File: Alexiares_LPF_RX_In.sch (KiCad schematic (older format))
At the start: 21 parts, among them J1 CONN_COAXIAL, J2 CONN_COAXIAL, J3 Conn_01x03, J5 CONN_COAXIAL

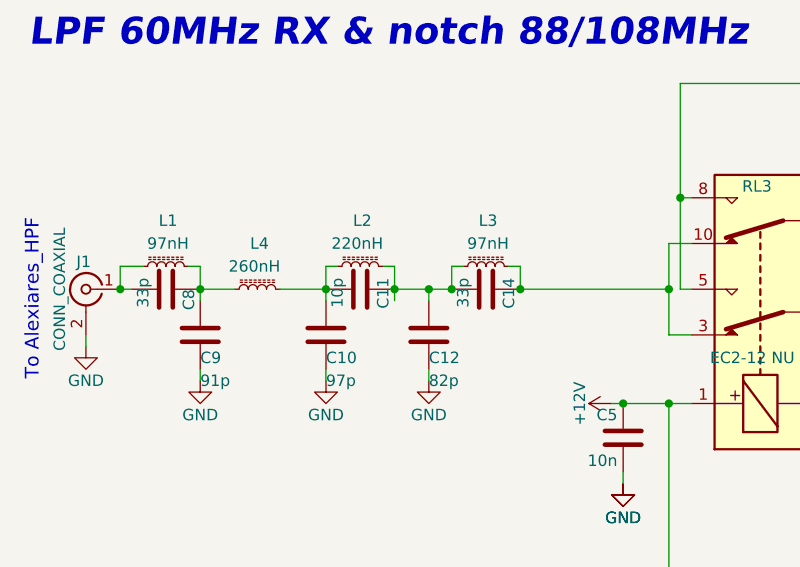
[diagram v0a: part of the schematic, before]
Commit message: Caps changed for ATC footprint
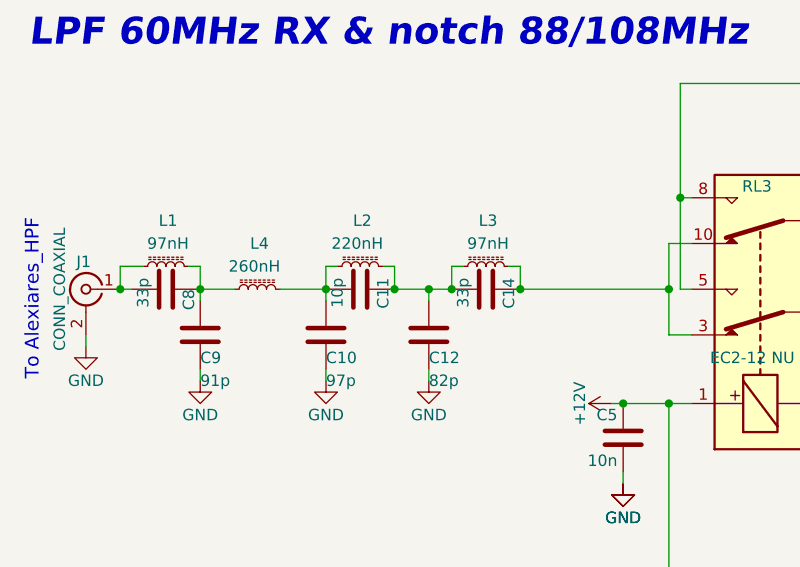
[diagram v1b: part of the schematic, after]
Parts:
- C10, C11, C12, C14, C8, C9: footprint Capacitors_SMD:C_1206_HandSoldering -> ATC_B:ATC_500_HandSoldering
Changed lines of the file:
@@
 F 0 "C14" H 3700 3900 50  0000 L CNN
 F 1 "33p" H 3700 3700 50  0000 L CNN
-F 2 "Capacitors_SMD:C_1206_HandSoldering" H 3788 3650 50  0001 C CNN
+F 2 "ATC_B:ATC_500_HandSoldering" H 3788 3650 50  0001 C CNN
 F 3 "" H 3750 3800 50  0000 C CNN
 	1    3750 3800
@@
 F 0 "C8" H 2350 3900 50  0000 L CNN
 F 1 "33p" H 2300 3700 50  0000 L CNN
-F 2 "Capacitors_SMD:C_1206_HandSoldering" H 2388 3650 50  0001 C CNN
+F 2 "ATC_B:ATC_500_HandSoldering" H 2388 3650 50  0001 C CNN
 F 3 "" H 2350 3800 50  0000 C CNN
 	1    2350 3800
@@
 F 0 "C11" H 3150 3900 50  0000 L CNN
 F 1 "10p" H 3150 3700 50  0000 L CNN
-F 2 "Capacitors_SMD:C_1206_HandSoldering" H 3238 3650 50  0001 C CNN
+F 2 "ATC_B:ATC_500_HandSoldering" H 3238 3650 50  0001 C CNN
 F 3 "" H 3200 3800 50  0000 C CNN
 	1    3200 3800
@@
 F 0 "C9" H 2500 3900 50  0000 L CNN
 F 1 "91p" H 2500 3800 50  0000 L CNN
-F 2 "Capacitors_SMD:C_1206_HandSoldering" H 2538 3850 50  0001 C CNN
+F 2 "ATC_B:ATC_500_HandSoldering" H 2538 3850 50  0001 C CNN
 F 3 "" H 2500 4000 50  0000 C CNN
 	1    2500 4000
@@
 F 0 "C10" H 3050 3900 50  0000 L CNN
 F 1 "97p" H 3050 3800 50  0000 L CNN
-F 2 "Capacitors_SMD:C_1206_HandSoldering" H 3088 3850 50  0001 C CNN
+F 2 "ATC_B:ATC_500_HandSoldering" H 3088 3850 50  0001 C CNN
 F 3 "" H 3050 4000 50  0000 C CNN
 	1    3050 4000
@@
 F 0 "C12" H 3500 3900 50  0000 L CNN
 F 1 "82p" H 3500 3800 50  0000 L CNN
-F 2 "Capacitors_SMD:C_1206_HandSoldering" H 3538 3850 50  0001 C CNN
+F 2 "ATC_B:ATC_500_HandSoldering" H 3538 3850 50  0001 C CNN
 F 3 "" H 3500 4000 50  0000 C CNN
 	1    3500 4000
@@
 Wire Wire Line
 	3050 3700 3050 3850
-Wire Wire Line
-	3350 3700 3350 3850
 Wire Wire Line
 	3350 3800 3600 3800
@@
 Text Notes 7600 4900 0    197  ~ 39
 Ajouter ferrites \nsur le relais
+Wire Wire Line
+	3350 3700 3350 3800
 $EndSCHEMATC

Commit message: DEPRECATED PROJECT, DO NOT USE WITH ALEX
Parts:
- added J4, J6, J7: CONN_COAXIAL, SMA_PINS:SMA_EDGE_NRW, symbol Conn_Coaxial
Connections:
- net GND: now also J4.2 (Ext), J6.2 (Ext), J7.2 (Ext)
- net at J2.1 (In), RL3.4, RL3.9: now also J7.1 (In)
- net at J5.1 (In), RL3.5, RL3.8: now also J6.1 (In)
- net at C8.2, J1.1 (In), L1.1: now also J4.1 (In)
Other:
- note added: "This project is deprecated\ndo no use on Angelia/Alexiares \n"
- note removed: "HPF \nOut"
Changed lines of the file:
@@
 Text Notes 8150 15900 0    60   ~ 0
 May 22nd 2017
-Text Notes 5700 3900 0    60   ~ 12
+Text Notes 6050 3900 0    60   ~ 12
 RX1_Line\n\n
-Text Notes 7800 14600 0    197  ~ 39
-HPF \nOut
+Text Notes 1700 2450 0    197  ~ 39
+This project is deprecated\ndo no use on Angelia/Alexiares \n
 Wire Wire Line
 	5500 4000 5500 4050
@@
 	3900 3800 4550 3800
 Wire Wire Line
-	2150 3700 2250 3700
+	1900 3700 2250 3700
 Wire Wire Line
 	2450 3700 2500 3700
@@
 	-1   0    0    -1
 $EndComp
-Text Notes 1800 4200 1    60   ~ 0
+Text Notes 1400 4050 1    60   ~ 0
 To Alexiares_HPF
 $Comp
@@
 Wire Wire Line
 	3350 3700 3350 3800
+Wire Wire Line
+	5300 3250 5300 3300
+$Comp
+L GND #PWR022
+U 1 1 5A34F329
+P 5300 3300
+F 0 "#PWR022" H 5300 3050 50  0001 C CNN
+F 1 "GND" H 5300 3150 50  0000 C CNN
+F 2 "" H 5300 3300 50  0000 C CNN
+F 3 "" H 5300 3300 50  0000 C CNN
+	1    5300 3300
+	-1   0    0    -1
+$EndComp
+$Comp
+L Conn_Coaxial J6
+U 1 1 5A34F32F
+P 5300 3050
+F 0 "J6" H 5310 3170 50  0000 C CNN
+F 1 "CONN_COAXIAL" V 5415 3050 50  0000 C CNN
+F 2 "SMA_PINS:SMA_EDGE_NRW" H 5300 3050 50  0001 C CNN
+F 3 "" H 5300 3050 50  0001 C CNN
+	1    5300 3050
+	1    0    0    -1
+$EndComp
+Wire Wire Line
+	5750 4000 5750 4050
+$Comp
+L GND #PWR023
+U 1 1 5A34F40A
+P 5750 4050
+F 0 "#PWR023" H 5750 3800 50  0001 C CNN
+F 1 "GND" H 5750 3900 50  0000 C CNN
+F 2 "" H 5750 4050 50  0000 C CNN
+F 3 "" H 5750 4050 50  0000 C CNN
+	1    5750 4050
+	-1   0    0    -1
+$EndComp
+$Comp
+L Conn_Coaxial J7
+U 1 1 5A34F410
+P 5750 3800
+F 0 "J7" H 5760 3920 50  0000 C CNN
+F 1 "CONN_COAXIAL" V 5865 3800 50  0000 C CNN
+F 2 "SMA_PINS:SMA_EDGE_NRW" H 5750 3800 50  0001 C CNN
+F 3 "" H 5750 3800 50  0001 C CNN
+	1    5750 3800
+	1    0    0    -1
+$EndComp
+Wire Wire Line
+	1750 4000 1750 4050
+$Comp
+L GND #PWR024
+U 1 1 5A34F599
+P 1750 4050
+F 0 "#PWR024" H 1750 3800 50  0001 C CNN
+F 1 "GND" H 1750 3900 50  0000 C CNN
+F 2 "" H 1750 4050 50  0000 C CNN
+F 3 "" H 1750 4050 50  0000 C CNN
+	1    1750 4050
+	1    0    0    -1
+$EndComp
+$Comp
+L Conn_Coaxial J4
+U 1 1 5A34F59F
+P 1750 3800
+F 0 "J4" H 1760 3920 50  0000 C CNN
+F 1 "CONN_COAXIAL" V 1865 3800 50  0000 C CNN
+F 2 "SMA_PINS:SMA_EDGE_NRW" H 1750 3800 50  0001 C CNN
+F 3 "" H 1750 3800 50  0001 C CNN
+	1    1750 3800
+	-1   0    0    -1
+$EndComp
+Wire Wire Line
+	5600 3800 5600 3650
+Wire Wire Line
+	5600 3650 5300 3650
+Connection ~ 5300 3650
+Wire Wire Line
+	5150 3050 5150 2900
+Connection ~ 5150 2900
+Wire Wire Line
+	1900 3800 1900 3700
+Connection ~ 2150 3700
 $EndSCHEMATC
